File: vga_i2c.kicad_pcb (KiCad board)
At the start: 2 copper layers, 87.9 x 77.2 mm, 34 parts, among them J1 VGA DB15 Female, J3 Atari 2600 Joystick DB9, J4 Conn_01x06, J5 Jumpers, J6 Conn_01x13, J7 VGA DB15 Female, SW1 SW_Push, SW2 SW_Push, SW3 SW_Push, SW4 SW Up, SW5 SW Down, SW6 SW Left, SW7 SW Right, SW8 SW Trigger, U1 MCP23017_SP

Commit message: !st production version.
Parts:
- removed SW4: SW Up, Buttons_Switches_ThroughHole:SW_PUSH_6mm
- removed SW5: SW Down, Buttons_Switches_ThroughHole:SW_PUSH_6mm
- removed SW6: SW Left, Buttons_Switches_ThroughHole:SW_PUSH_6mm
- removed SW7: SW Right, Buttons_Switches_ThroughHole:SW_PUSH_6mm
- removed SW8: SW Trigger, Buttons_Switches_ThroughHole:SW_PUSH_6mm
- U1: value MCP23017_SP -> MCP23017_SO; footprint Housings_DIP:DIP-28_W7.62mm_LongPads -> Housings_SOIC:SOIC-28W_7.5x18.7mm_Pitch1.27mm
- moved J3 51.2 mm to (80.5, 65.8), turned to 180 degrees
- moved R10 45.5 mm to (96.2, 97.0)
- moved R12 43.8 mm to (82.9, 97.0), turned to 180 degrees
- moved R11 43.1 mm to (87.2, 97.0)
- moved SW3 41.6 mm to (83.1, 101.1)
- moved C2 35.0 mm to (98.3, 84.8)
- moved J4 34.9 mm to (52.3, 99.3), turned to 90 degrees
- moved J5 29.7 mm to (54.9, 94.7), turned to 90 degrees
- moved R8 28.9 mm to (68.8, 95.8), turned to 0 degrees
- moved SW1 27.9 mm to (105.4, 101.1)
- moved R7 26.5 mm to (68.8, 93.7), turned to 0 degrees
- moved SW2 25.8 mm to (94.2, 101.1)
- moved D1 21.2 mm to (110.8, 95.6), turned to 180 degrees
- moved R6 21.0 mm to (91.9, 103.0), turned to 90 degrees
- moved R14 20.9 mm to (91.6, 97.0), turned to 180 degrees
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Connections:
- net Net-(R9-Pad1) renamed /rstn
- U1 pad 21: /up -> /right
- U1 pad 22: /down -> /left
- U1 pad 23: /left -> /down
- U1 pad 24: /right -> /trigger
- U1 pad 25: /trigger -> /up
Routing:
- net GND: track 256.7 -> 35.0 mm, vias 2 -> 3
- net +5V: track 343.7 -> 197.7 mm
- net /down: track 97.0 -> 34.5 mm
- net /left: track 90.0 -> 36.0 mm
- net Net-(J6-Pad4): track 80.7 -> 34.2 mm, vias 2 -> 1
- net /rsvd0_m: track 68.7 -> 114.4 mm, vias 1 -> 0
- net /up: track 79.8 -> 34.2 mm
- net /rsvd2_m: track 52.6 -> 93.5 mm, vias 1 -> 0
- net /ddc_sda_m: track 104.0 -> 141.0 mm, vias 2 -> 0
- net /ddc_scl_m: track 143.2 -> 106.7 mm, vias 0 -> 2
- net /trigger: track 70.0 -> 35.8 mm, vias 0 -> 1
- net Net-(J6-Pad3): track 64.8 -> 32.4 mm, vias 2 -> 1
- net Net-(J6-Pad2): track 64.6 -> 36.7 mm
- net /right: track 69.3 -> 42.6 mm
- net /rsvd0_f: track 41.6 -> 15.9 mm
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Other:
- board size 87.9 x 77.2 mm -> 69.8 x 54.1 mm

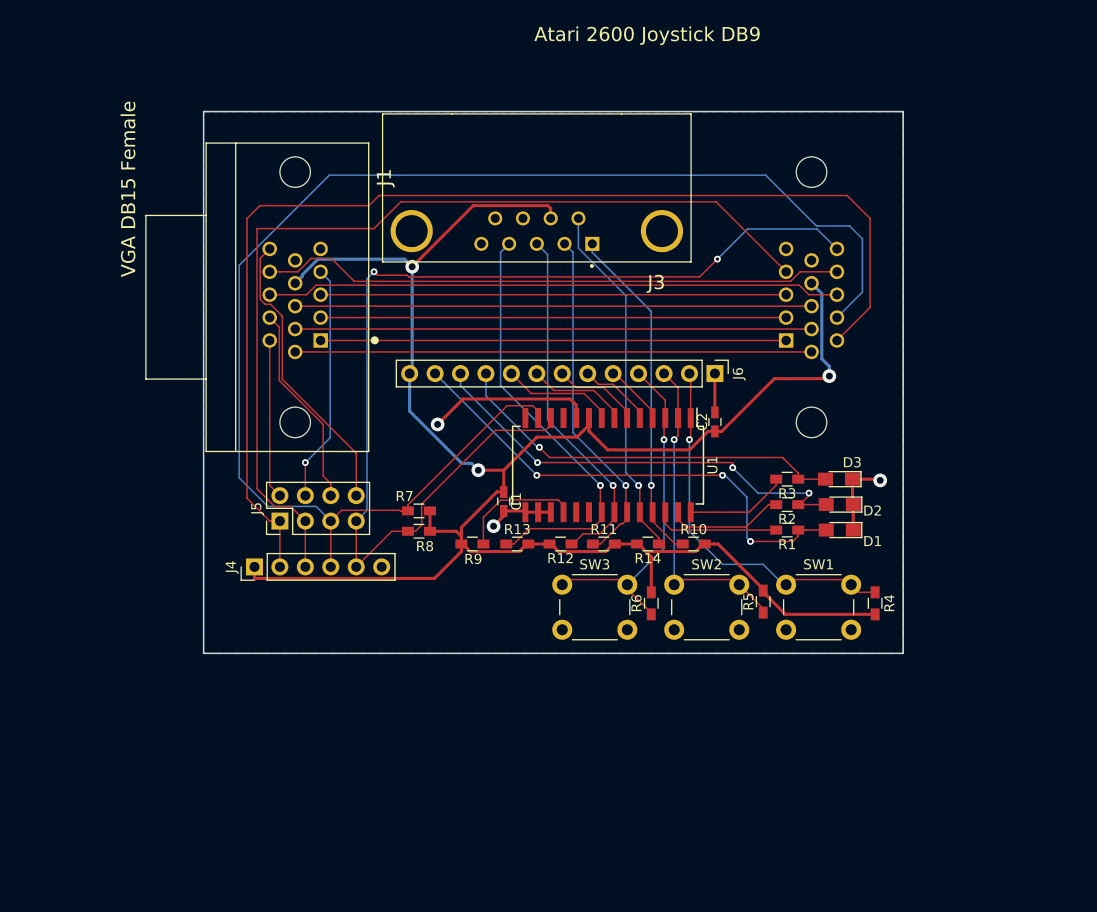
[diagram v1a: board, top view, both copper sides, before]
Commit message: Version with 2 joysticks.
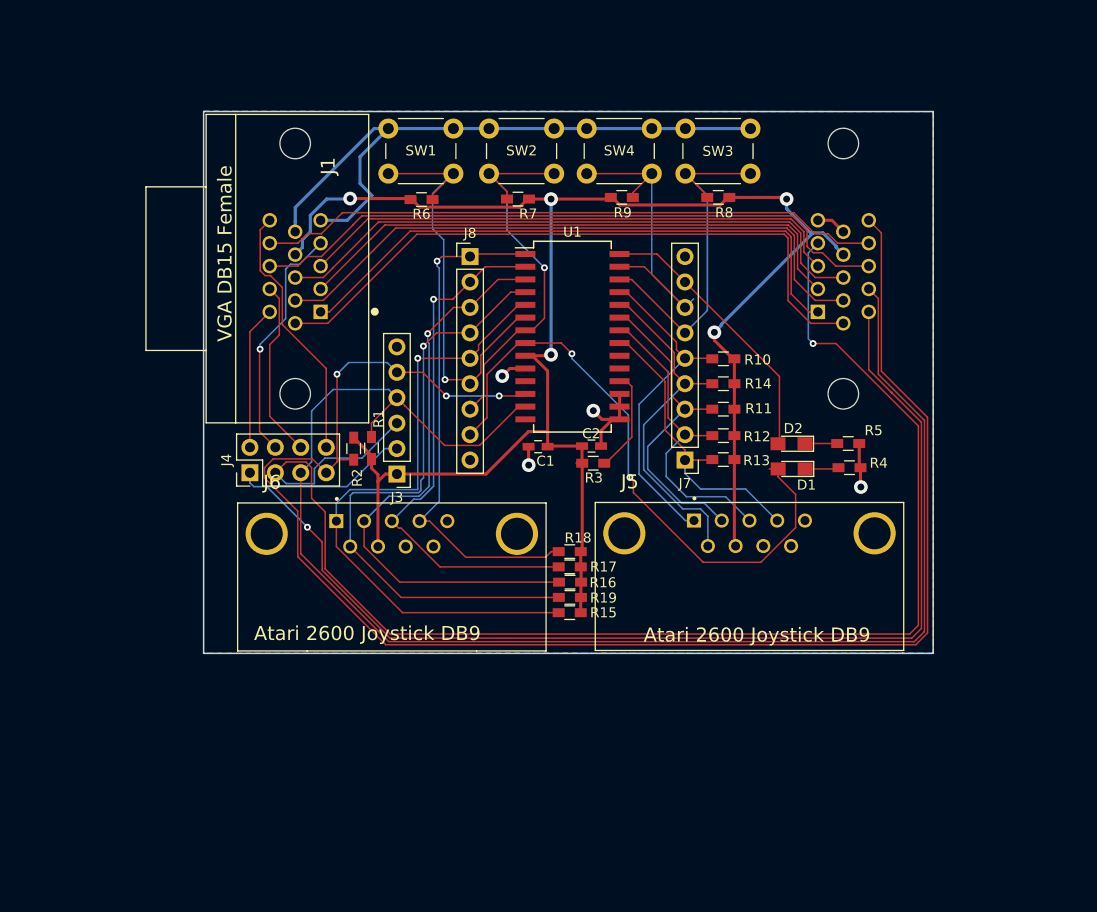
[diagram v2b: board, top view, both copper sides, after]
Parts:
- removed D3: LED, LEDs:LED_0805_HandSoldering
- added J2: VGA DB15 Female, 181-015-213R561:NORCOMP_181-015-213R561, B.Cu at (111.1, 69.5)
- added J8: Conn_01x09, Pin_Headers:Pin_Header_Straight_1x09_Pitch2.54mm, F.Cu at (73.9, 68.3)
- added R15: 10K, Resistors_SMD:R_0603_HandSoldering, F.Cu at (83.8, 103.9)
- added R16: 10K, Resistors_SMD:R_0603_HandSoldering, F.Cu at (83.8, 100.8)
- added R17: 10K, Resistors_SMD:R_0603_HandSoldering, F.Cu at (83.8, 99.3)
- added R18: 10K, Resistors_SMD:R_0603_HandSoldering, F.Cu at (83.8, 97.8)
- added R19: 10K, Resistors_SMD:R_0603_HandSoldering, F.Cu at (83.8, 102.4)
- added SW4: SW_Push, Buttons_Switches_ThroughHole:SW_PUSH_6mm, F.Cu at (92.0, 60.0)
- J3: value Atari 2600 Joystick DB9 -> Conn_01x06; footprint 1-1634580-2:TE_1-1634580-2 -> Pin_Headers:Pin_Header_Straight_1x06_Pitch2.54mm
- J4: value Conn_01x06 -> Jumpers; footprint Pin_Headers:Pin_Header_Straight_1x06_Pitch2.54mm -> Pin_Headers:Pin_Header_Straight_2x04_Pitch2.54mm
- J5: value Jumpers -> Atari 2600 Joystick DB9; footprint Pin_Headers:Pin_Header_Straight_2x04_Pitch2.54mm -> 1-1634580-2:TE_1-1634580-2
- J6: value Conn_01x13 -> Atari 2600 Joystick DB9; footprint Pin_Headers:Pin_Header_Straight_1x13_Pitch2.54mm -> 1-1634580-2:TE_1-1634580-2
- J7: value VGA DB15 Female -> Conn_01x09; footprint 181-015-213R561:NORCOMP_181-015-213R561 -> Pin_Headers:Pin_Header_Straight_1x09_Pitch2.54mm; moved to F.Cu
- R1, R2: value 330 -> NS
- R3: value 330 -> 10K
- R4, R5: value 10K -> 330
- R7, R8: value NS -> 10K
- moved SW1 52.8 mm to (72.2, 60.0), turned to 180 degrees
- moved J5 46.9 mm to (101.8, 96.0), turned to 0 degrees
- moved R6 46.4 mm to (69.0, 62.6), turned to 180 degrees
- moved SW3 45.1 mm to (101.9, 60.0), turned to 180 degrees
- moved R8 44.8 mm to (98.6, 62.4)
- moved R2 43.6 mm to (62.2, 87.5), turned to 90 degrees
- moved SW2 42.8 mm to (82.2, 60.0), turned to 180 degrees
- moved R1 42.3 mm to (64.0, 87.4), turned to 270 degrees
- moved R9 37.7 mm to (89.0, 62.4)
- moved J6 36.0 mm to (66.0, 96.0), turned to 0 degrees
- moved R7 32.7 mm to (78.6, 62.6)
- moved J3 28.0 mm to (66.5, 90.0)
- moved R13 22.2 mm to (99.1, 88.6)
- moved J7 20.6 mm to (95.3, 88.6), turned to 180 degrees
- moved R12 19.5 mm to (99.1, 86.2), turned to 0 degrees
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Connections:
- D1 pad 1: GND -> Net-(D1-Pad1)
- D1 pad 2: Net-(D1-Pad2) -> /led1_2
- D2 pad 1: GND -> Net-(D2-Pad1)
- D2 pad 2: Net-(D2-Pad2) -> /led1
- J3 pad 1: /up -> +5V
- J3 pad 2: /down -> /rsvd0_m
- J3 pad 3: /left -> /rsvd2_m
- J3 pad 4: /right -> /ddc_sda_m
- J3 pad 5: /paddle_b -> /ddc_scl_m
- J3 pad 6: /trigger -> GND
- J4 pad 1: +5V -> /rsvd0_m
- J4 pad 2: /rsvd0_m -> /rsvd0_f
- J4 pad 4: /ddc_sda_m -> /rsvd2_f
- J4 pad 5: /ddc_scl_m -> /ddc_sda_m
- J4 pad 6: GND -> /ddc_sda_f
- J5 pad 1: /rsvd0_m -> /up
- J5 pad 2: /rsvd0_f -> /down
- J5 pad 3: /rsvd2_m -> /left
- J5 pad 4: /rsvd2_f -> /right
- J5 pad 5: /ddc_sda_m -> /paddle_b
- J5 pad 6: /ddc_sda_f -> /trigger
- J5 pad 7: /ddc_scl_m -> +5V
- J5 pad 8: /ddc_scl_f -> GND
- J6 pad 1: GND -> /up_2
- J6 pad 2: Net-(J6-Pad2) -> /down_2
- J6 pad 3: Net-(J6-Pad3) -> /left_2
- J6 pad 4: Net-(J6-Pad4) -> /right_2
- J6 pad 5: Net-(J6-Pad5) -> /paddle_b_2
- J6 pad 6: Net-(J6-Pad6) -> /trigger_2
- J6 pad 7: Net-(J6-Pad7) -> +5V
- J6 pad 8: Net-(J6-Pad8) -> GND
- J6 pad 9: Net-(J6-Pad9) -> /paddle_a_2
- J7 pad 1: /red -> /right
- J7 pad 2: /green -> /left
- J7 pad 3: /blue -> /down
- J7 pad 4: /rsvd2_m -> /trigger
- J7 pad 5: GND -> /up
- J7 pad 6: /red_ret -> /sw1
- J7 pad 7: /green_ret -> /sw2
- J7 pad 8: /blue_ret -> /led1
- J7 pad 9: +5V -> GND
- R1 pad 1: Net-(D1-Pad2) -> /ddc_sda_m
- R1 pad 2: Net-(R1-Pad2) -> +5V
- R2 pad 1: Net-(D2-Pad2) -> /ddc_scl_m
- R2 pad 2: Net-(R2-Pad2) -> +5V
- R3 pad 1: Net-(D3-Pad2) -> /rstn
- R3 pad 2: Net-(R3-Pad2) -> +5V
- R4 pad 1: Net-(J6-Pad2) -> GND
- R4 pad 2: +5V -> Net-(D1-Pad1)
- R5 pad 1: Net-(J6-Pad3) -> GND
- R5 pad 2: +5V -> Net-(D2-Pad1)
- R6 pad 1: Net-(J6-Pad4) -> /sw1_2
- R7 pad 1: /ddc_sda_m -> /sw2_2
- R8 pad 1: /ddc_scl_m -> /sw1
- R9 pad 1: /rstn -> /sw2
- SW1 pad 1: Net-(J6-Pad2) -> /sw1_2
- SW2 pad 1: Net-(J6-Pad3) -> /sw2_2
- SW3 pad 1: Net-(J6-Pad4) -> /sw1
- U1 pad 1: Net-(J6-Pad2) -> /right_2
- U1 pad 2: Net-(J6-Pad3) -> /left_2
- U1 pad 26: Net-(R1-Pad2) -> /sw1
- U1 pad 27: Net-(R2-Pad2) -> /sw2
- U1 pad 28: Net-(R3-Pad2) -> /led1
- U1 pad 3: Net-(J6-Pad4) -> /down_2
- U1 pad 4: Net-(J6-Pad5) -> /trigger_2
- U1 pad 5: Net-(J6-Pad6) -> /up_2
- U1 pad 6: Net-(J6-Pad7) -> /sw1_2
- U1 pad 7: Net-(J6-Pad8) -> /sw2_2
- U1 pad 8: Net-(J6-Pad9) -> /led1_2
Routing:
- net /up_2: track 0.00 -> 64.3 mm, vias 0 -> 1
- net /trigger_2: track 0.00 -> 62.2 mm, vias 0 -> 1
- net /led1_2: track 0.00 -> 61.3 mm, vias 0 -> 2
- net /down_2: track 0.00 -> 58.7 mm, vias 0 -> 1
- net /ddc_scl_m: track 106.7 -> 160.8 mm, vias 2 -> 3
- net /left_2: track 0.00 -> 53.3 mm, vias 0 -> 1
- net GND: track 35.0 -> 87.3 mm, vias 3 -> 4
- net /right_2: track 0.00 -> 51.6 mm, vias 0 -> 1
- net Net-(D1-Pad2): track 49.2 -> 0.00 mm, vias 3 -> 0
- net Net-(D2-Pad2): track 45.2 -> 0.00 mm, vias 3 -> 0
- net /rsvd2_m: track 93.5 -> 137.7 mm, vias 0 -> 1
- net /sw1_2: track 0.00 -> 43.9 mm, vias 0 -> 1
- net Net-(D3-Pad2): track 39.9 -> 0.00 mm, vias 1 -> 0
- net /sw2_2: track 0.00 -> 39.5 mm, vias 0 -> 1
- net Net-(J6-Pad2): track 36.7 -> 0.00 mm, vias 1 -> 0
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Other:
- board size 69.8 x 54.1 mm -> 72.8 x 54.1 mm
